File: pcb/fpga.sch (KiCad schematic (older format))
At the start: 54 parts, among them J1 CONN_INTEGRALSTICK_FPGA_DEVICE, Q1 SSM6N58NU, Q2 SSM6N58NU, Q3 SSM6N58NU, U12 DSC6001HI2A-025.0000‎, U2 XC7A50T-1FTG256C, U9 AT24MAC402-UDFN

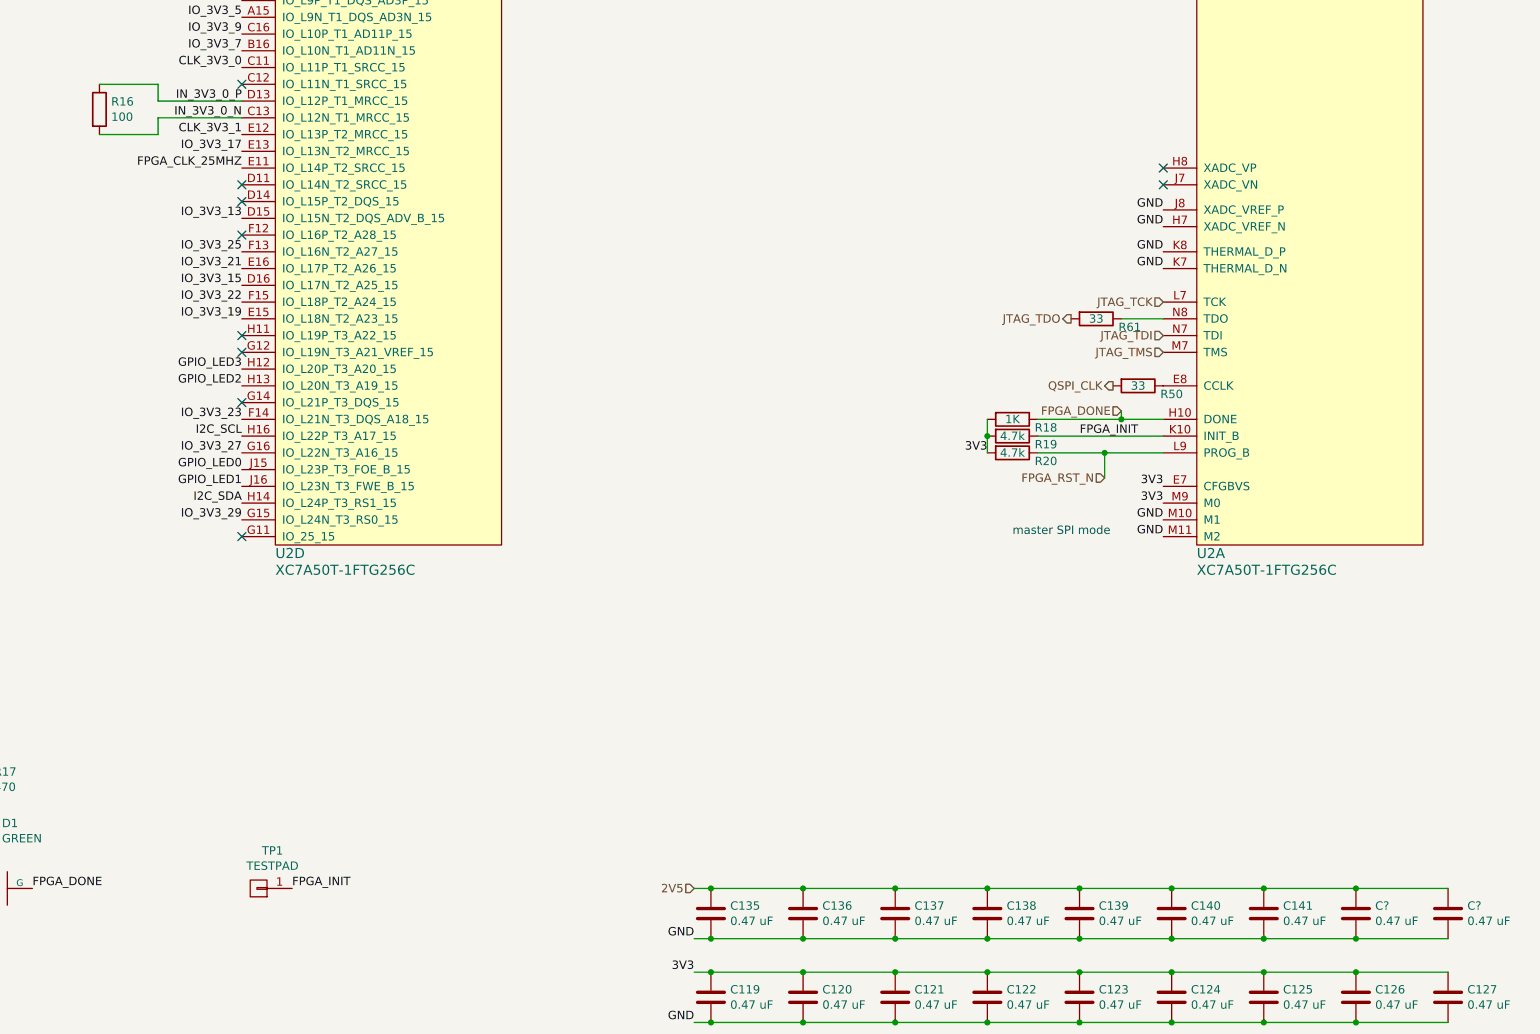
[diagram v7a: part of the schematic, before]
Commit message: Continued FPGA layout. Fanned out most signals going to MCU but pin assignments aren't final.
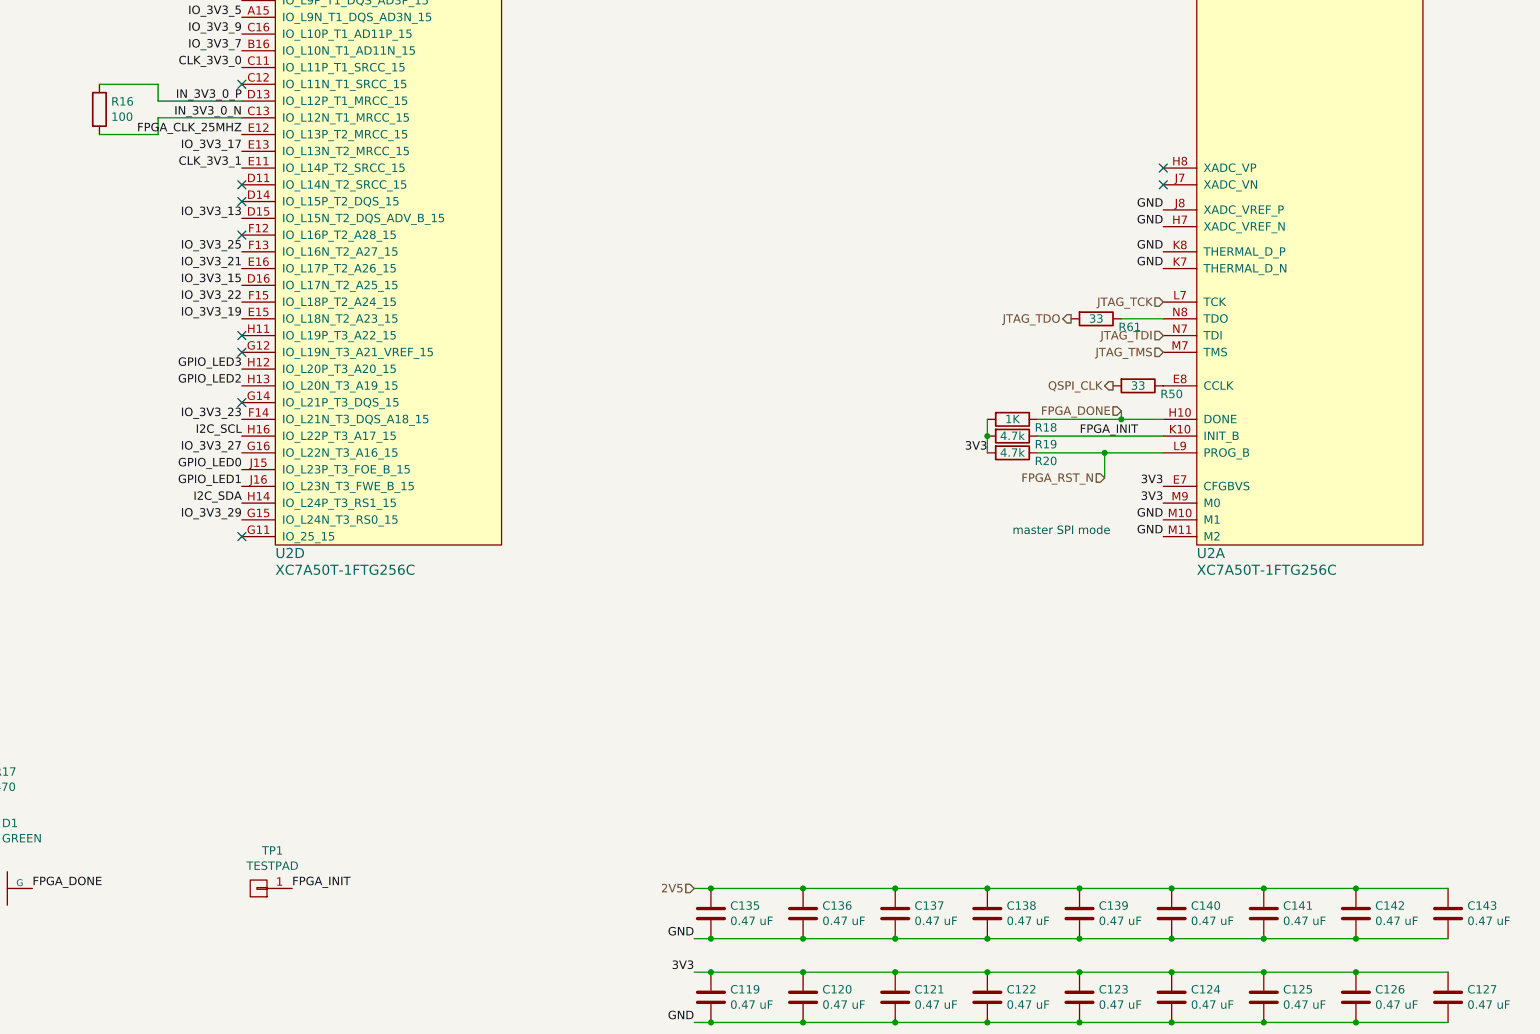
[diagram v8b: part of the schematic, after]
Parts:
- gave numbers to parts that had none: 2
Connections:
- net CLK_3V3_1: now also U2.E11 (IO_L14P_T2_SRCC_15); no longer U2.E12 (IO_L13P_T2_MRCC_15)
- net FPGA_CLK_25MHZ: now also U2.E12 (IO_L13P_T2_MRCC_15); no longer U2.E11 (IO_L14P_T2_SRCC_15)
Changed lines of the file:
@@
 Sheet 6 8
 Title "INTEGRALSTICK Compute Module"
-Date "2018-11-13"
+Date "2018-11-14"
 Rev "0.1"
 Comp "Andrew D. Zonenberg"
@@
 Text Label 8400 2850 2    50   ~ 0
 CLK_3V3_0
-Text Label 8400 3250 2    50   ~ 0
+Text Label 8400 3450 2    50   ~ 0
 CLK_3V3_1
 Text Label 8400 1050 2    50   ~ 0
@@
 Wire Wire Line
 	3050 7000 3050 7100
-Text Label 8400 3450 2    50   ~ 0
+Text Label 8400 3250 2    50   ~ 0
 FPGA_CLK_25MHZ
 Text HLabel 8400 850  0    50   Input ~ 0
@@
 P 15050 7900
 AR Path="/5B6B7044/5C3E05B4" Ref="C?"  Part="1"
-AR Path="/5B6B702C/5C3E05B4" Ref="C?"  Part="1"
-F 0 "C?" H 15165 7946 50  0000 L CNN
+AR Path="/5B6B702C/5C3E05B4" Ref="C142"  Part="1"
+F 0 "C142" H 15165 7946 50  0000 L CNN
 F 1 "0.47 uF" H 15165 7855 50  0000 L CNN
 F 2 "azonenberg_pcb:EIA_0402_CAP_NOSILK" H 15088 7750 50  0001 C CNN
@@
 P 15600 7900
 AR Path="/5B6B7044/5C3E0A0B" Ref="C?"  Part="1"
-AR Path="/5B6B702C/5C3E0A0B" Ref="C?"  Part="1"
-F 0 "C?" H 15715 7946 50  0000 L CNN
+AR Path="/5B6B702C/5C3E0A0B" Ref="C143"  Part="1"
+F 0 "C143" H 15715 7946 50  0000 L CNN
 F 1 "0.47 uF" H 15715 7855 50  0000 L CNN
 F 2 "azonenberg_pcb:EIA_0402_CAP_NOSILK" H 15638 7750 50  0001 C CNN
